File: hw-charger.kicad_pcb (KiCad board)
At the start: 4 copper layers, 100 x 65 mm, 147 parts, among them J10 Screw_Terminal_01x02, J17 Conn_01x02, J19 Conn_01x02, J2 Conn_02x04_Odd_Even, J27 Conn_01x05, J3 Screw_Terminal_01x03, J4 Conn_02x05_Odd_Even, J56 Screw_Terminal_01x02, J57 Conn_01x02, J58 Screw_Terminal_01x02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

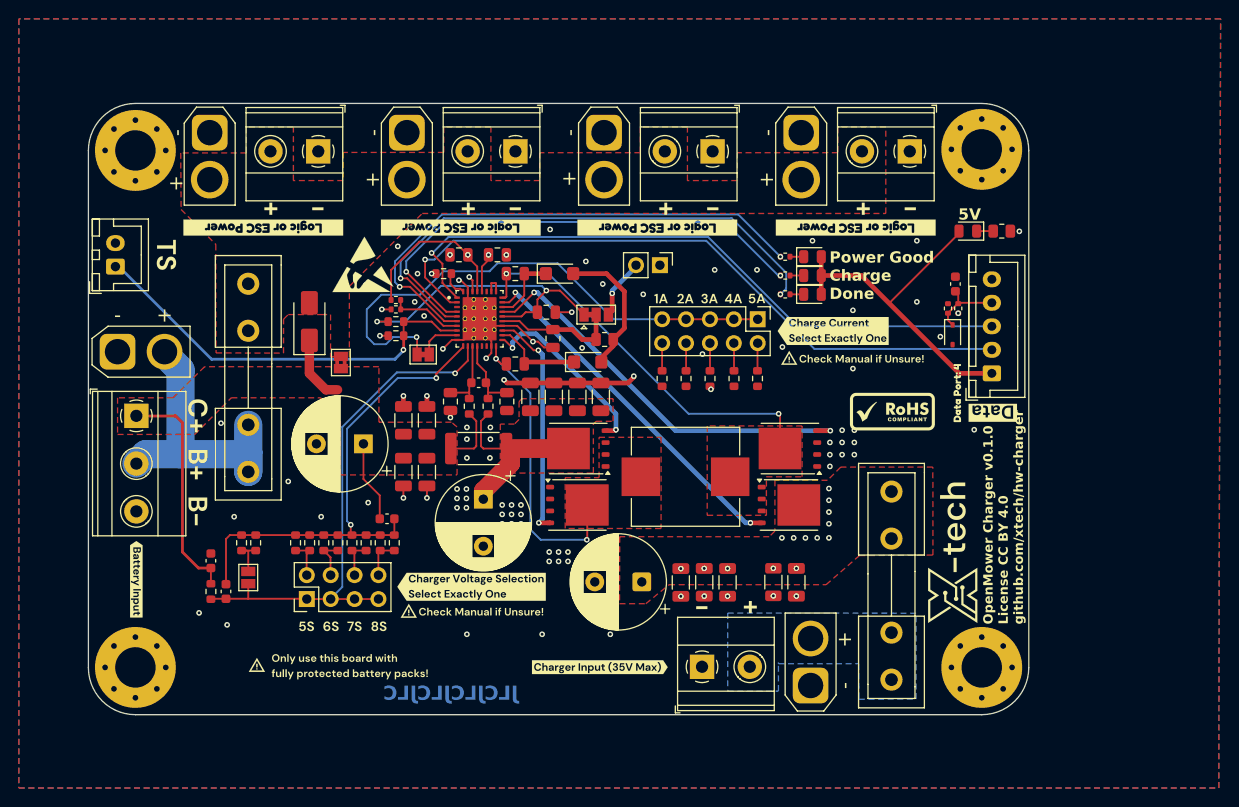
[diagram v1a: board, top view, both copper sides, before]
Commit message: Add AC-Sense
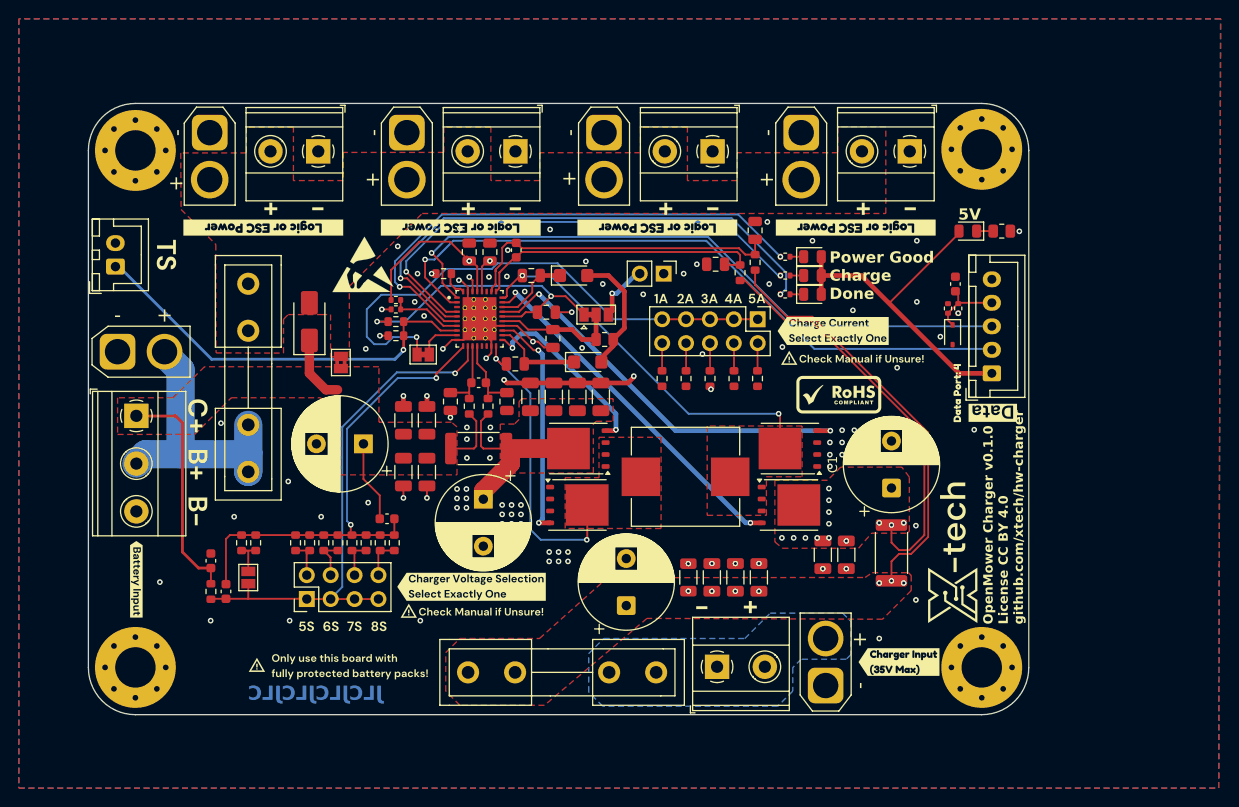
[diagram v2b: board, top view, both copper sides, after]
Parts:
- removed kibuzzard-6853DB41: G***, kibuzzard-6853DB41
- added C1: 220uF@80V, Capacitor_THT:CP_Radial_D10.0mm_P5.00mm, F.Cu at (130.4, 175.7)
- added C2: 4.7uF@50V, Capacitor_SMD:C_1206_3216Metric, F.Cu at (111.3, 185.2)
- added C62: 100nF@100V, Capacitor_SMD:C_0805_2012Metric, F.Cu at (115.9, 148.3)
- added C77: 100nF@100V, Capacitor_SMD:C_0805_2012Metric, F.Cu at (111.7, 151.9)
- added C85: 470nF/25V, Capacitor_SMD:C_0603_1608Metric, F.Cu at (90.5, 150.4)
- added R1: 10R, Resistor_SMD:R_0603_1608Metric, F.Cu at (115.9, 151.7)
- added R3: 10R, Resistor_SMD:R_0603_1608Metric, F.Cu at (114.3, 152.8)
- added R30: 5m, Resistor_SMD:R_2512_6332Metric, F.Cu at (130.4, 182.6)
- added kibuzzard-69CD6E52: G***, kibuzzard-69CD6E52, F.Cu at (131.2, 194.2)
- R67: value 5mR -> 5m
- R74: value 133kR -> 133k
- moved U15 45.7 mm to (87.9, 195.3), turned to 90 degrees
- moved U74 36.2 mm to (95.4, 195.3), turned to 0 degrees
- moved U17 27.6 mm to (102.9, 195.3), turned to 90 degrees
- moved F2 25.0 mm to (105.4, 195.3), turned to 180 degrees
- moved C41 17.8 mm to (125.6, 182.8)
- moved C39 12.9 mm to (123.1, 182.8)
- moved R22 9.05 mm to (108.8, 185.2), turned to 90 degrees
- moved C40 6.51 mm to (113.8, 185.2), turned to 90 degrees
- moved REF** 5.98 mm to (124.8, 169.8)
- moved C38 3.37 mm to (116.3, 185.2), turned to 90 degrees
- moved C42 3.01 mm to (102.2, 188.2), turned to 90 degrees
- moved C13 1.71 mm to (92.1, 153.1)
- moved J10 1.60 mm to (111.9, 194.7)
- moved J17 1.60 mm to (123.4, 196.7)
- moved D26 1.51 mm to (96.6, 153.1)
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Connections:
- C39 pad 1: /V_CHARGE -> Net-(Q6-D)
- C41 pad 1: /V_CHARGE -> Net-(Q6-D)
- Q6 pad 5: /V_CHARGE -> Net-(Q6-D)
- U27 pad 30: Net-(U27-ACN) -> Net-(U27-ACP)
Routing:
- net /V_CHARGE: track 91.6 -> 147.8 mm, vias 18 -> 11
- net Net-(Q6-D): track 0.00 -> 43.5 mm, vias 0 -> 13
- net Net-(U27-ACP): track 0.00 -> 34.4 mm
- net Net-(U27-ACN): track 2.27 -> 31.3 mm
- net Net-(D2-A): track 14.3 -> 12.7 mm
- net Net-(Q7-D): track 41.8 -> 40.5 mm
- net Net-(D26-K): track 7.48 -> 8.14 mm
- net /Charger/REGN: track 32.6 -> 32.1 mm
- net GND: vias 113 -> 124
- added copper zone on F.Cu, net Net-(Q6-D)
- added copper zone on In2.Cu, net Net-(Q6-D)

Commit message: Add /CE, NTC Selector, 5V LDO. Fix copper traces, vias in pads and this and that
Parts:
- removed R79: 1k, Resistor_SMD:R_0805_2012Metric
- removed kibuzzard-671117D8: G***, kibuzzard-671117D8
- removed kibuzzard-671119EE: G***, kibuzzard-671119EE
- removed kibuzzard-6711201C: G***, kibuzzard-6711201C
- removed kibuzzard-6853DB1B: G***, kibuzzard-6853DB1B
- removed the kibuzzard-69C99438 at (63.6, 148.0)
- added C3: 4.7uF@50V, Capacitor_SMD:C_1206_3216Metric, F.Cu at (133.3, 162.2)
- added C6: 4.7uF@50V, Capacitor_SMD:C_1206_3216Metric, F.Cu at (133.3, 155.7)
- added C7: 100nF@50V, Capacitor_SMD:C_0603_1608Metric, F.Cu at (130.1, 155.7)
- added R5: 10k, Resistor_SMD:R_0402_1005Metric, F.Cu at (53.2, 158.2)
- added R6: 10k, Resistor_SMD:R_0402_1005Metric, F.Cu at (117.5, 151.0)
- added TP2: TestPoint_2Pole, Connector_PinHeader_2.54mm:PinHeader_1x02_P2.54mm_Vertical, F.Cu at (106.2, 152.9)
- added TP3: TS Select, Connector_PinHeader_2.54mm:PinHeader_1x03_P2.54mm_Vertical, F.Cu at (61.5, 194.8)
- added U1: ME6203A50M3G, easyeda2kicad:SOT-23-3_L2.9-W1.6-P1.90-LS2.8-BR, F.Cu at (133.3, 159.0)
- added U2: Jumper Black, xtech:SNT-100-BK-H, F.Cu at (60.3, 194.8)
- added U3: Jumper Black, xtech:SNT-100-BK-H, F.Cu at (53.7, 151.9)
- added kibuzzard-69CEE1A3: G***, kibuzzard-69CEE1A3, F.Cu at (63.6, 148.0)
- added kibuzzard-69CEE455: G***, kibuzzard-69CEE455, F.Cu at (50.1, 186.7)
- added kibuzzard-69CEEB52: G***, kibuzzard-69CEEB52, F.Cu at (72.3, 192.9)
- added kibuzzard-69CFD05E: G***, kibuzzard-69CFD05E, F.Cu at (141.6, 148.1)
- added kibuzzard-69CFD081: G***, kibuzzard-69CFD081, F.Cu at (48.4, 148.2)
- F1, F2: footprint local_FUSE:Fuseholder5x20_horiz_open_inline_Type-I -> local_FUSE:Fuseholder5x20_horiz_open_inline_C3130
- R72: value 5.24kR -> 5k1/1%
- R73: value 30.31kR -> 30k/1%
- TP1: value TestPoint_2Pole -> TS Select; footprint Connector_PinHeader_2.54mm:PinHeader_1x02_P2.54mm_Vertical -> Connector_PinHeader_2.54mm:PinHeader_1x03_P2.54mm_Vertical
- U72: footprint xtech:Dummy -> xtech:SNT-100-RD-G
- U73: footprint xtech:Dummy -> xtech:SNT-100-BL-H
- moved REF** 56.7 mm to (77.4, 201.0)
- moved TP1 52.5 mm to (53.7, 150.7), turned to 0 degrees
- moved R75 41.5 mm to (63.9, 195.8), turned to -90 degrees
- moved R21 40.5 mm to (63.9, 193.8), turned to 90 degrees
- moved C62 21.7 mm to (94.2, 148.2)
- moved R1 19.2 mm to (96.8, 149.7), turned to 180 degrees
- moved D39 18.8 mm to (119.9, 151.0), turned to 0 degrees
- moved C77 18.6 mm to (93.1, 151.9)
- moved R3 17.6 mm to (96.8, 151.2), turned to 180 degrees
- moved R55 12.0 mm to (141.2, 167.6), turned to 180 degrees
- moved R54 11.1 mm to (139.2, 167.6), turned to 180 degrees
- moved D23 7.21 mm to (139.8, 166.0), turned to 0 degrees
- moved kibuzzard-69C99648 3.90 mm to (137.4, 161.7)
- moved kibuzzard-670E90ED 3.08 mm to (124.8, 163.8)
- moved kibuzzard-6711AB8A 2.83 mm to (122.1, 160.9)
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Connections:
- J19 pad 1: /Charger/TS -> /Charger/NTC_BATT
- J27 pad 1: /5V -> unconnected-(J27-Pin_1-Pad1)
- R21 pad 2: Net-(U27-~{CE}) -> Net-(TP3-C)
- R75 pad 1: Net-(U27-~{CE}) -> Net-(TP3-A)
- TP1 pad 1: GND -> /Charger/NTC_BATT
- TP1 pad 2: Net-(JP1-B) -> /Charger/TS
- U27 pad 7: Net-(U27-~{CE}) -> Net-(TP3-C)
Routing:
- net Net-(TP3-C): track 0.00 -> 55.0 mm, vias 0 -> 2
- net Net-(U27-ACP): track 34.4 -> 13.0 mm
- net Net-(U27-ACN): track 31.3 -> 10.6 mm
- net /V_CHARGE: track 147.8 -> 166.2 mm, vias 11 -> 13
- net Net-(Q6-D): track 43.5 -> 61.4 mm
- net /5V: track 37.0 -> 19.4 mm
- net /V_CHARGE_SENSE: track 7.39 -> 17.6 mm
- net Net-(J4-Pin_1): track 56.8 -> 48.9 mm
- net Net-(U27-~{CE}): track 7.71 -> 0.00 mm
- net /Charger/NTC_BATT: track 0.00 -> 7.38 mm
- net /Charger/TS: track 43.6 -> 36.7 mm
- net GND: track 41.4 -> 35.5 mm, vias 124 -> 138
- net /Charger/V_BATT_CHARGE: track 46.5 -> 41.8 mm
- net Net-(J3-Pin_2): track 30.9 -> 27.3 mm
- net Net-(TP3-A): track 0.00 -> 2.60 mm
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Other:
- board text added: "5V Charge Pwr Good Charge Done"
- board text added: "Charger v0.1.0 License CC BY 4.0 github.com/xtech/hw-charger"
- board text added: "Enable by"
- board text added: "HW | SW"
- board text added: "NTC | Off"
- board text removed: "5V"
- board text removed: "JLCJLCJLCJLC"
- board text removed: "OpenMower Charger v0.1.0 License CC BY 4.0 github.com/xtech/hw-charger"
- board text removed: "Power Good Charge Done"
